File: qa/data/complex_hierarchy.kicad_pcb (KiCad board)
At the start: 2 copper layers, 72 parts, among them P1 CONN_2, P2 CONN_2, P3 CONN_2, P4 CONN_2, P5 CONN_2, P6 CONN_2, Q1 MPAS92, Q2 MPAS42, Q3 MPAS92, Q4 MPAS42, Q5 MPAS92, Q6 MPAS42, Q7 MPAS92, Q8 MPAS42, U1 ICL7660, U2 78L05, U3 LM358N, U4 LM358N

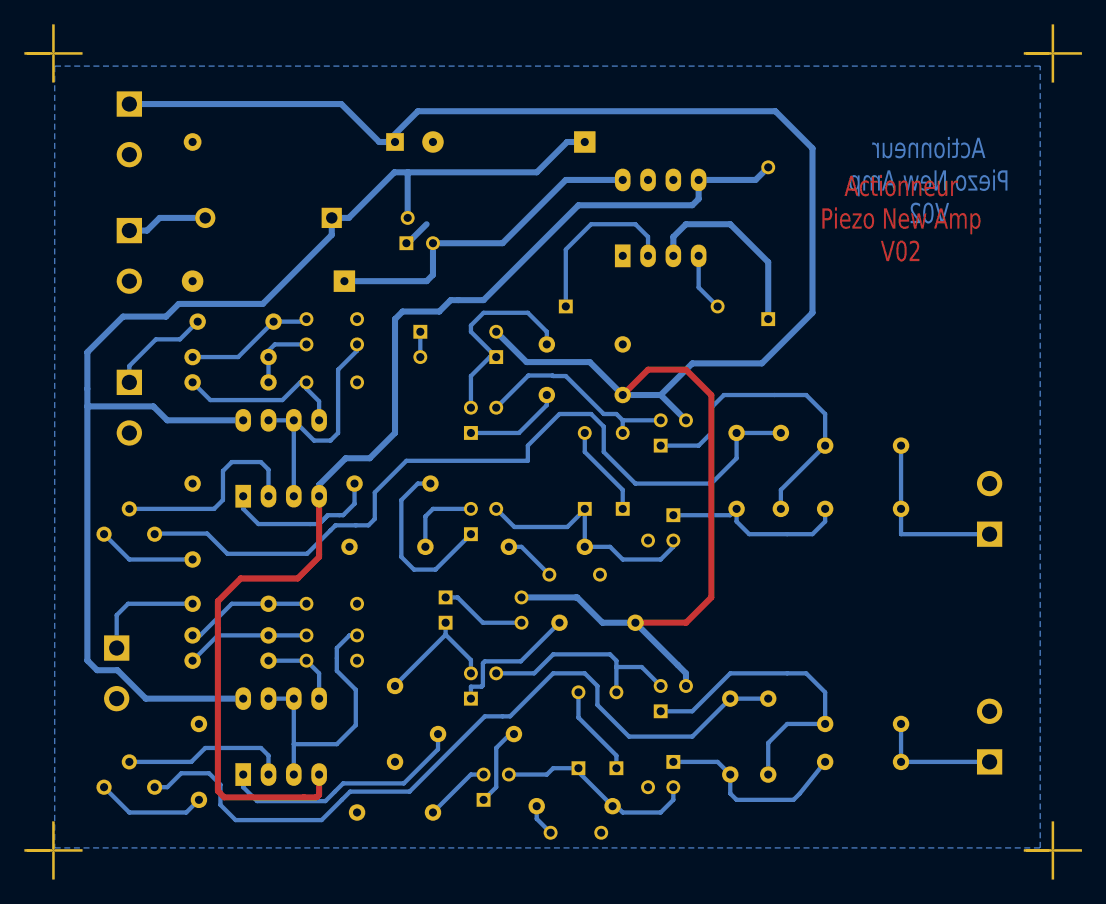
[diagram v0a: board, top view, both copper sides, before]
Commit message: Update complex_hierarchy.kicad_pcb file, used in qa tests, which was created by a test version of Pcbnew, and was not currently readable.
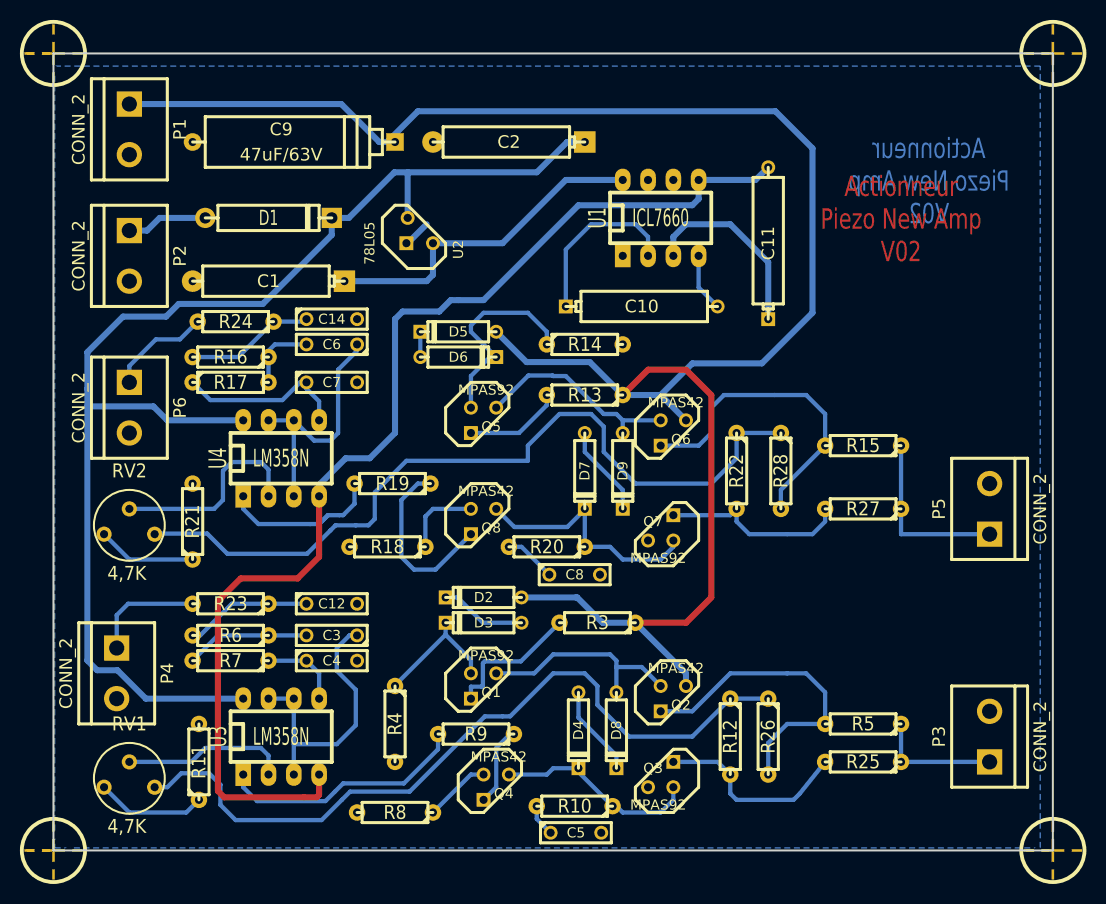
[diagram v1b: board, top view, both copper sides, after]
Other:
- board outline added: 100.3 x 80 mm
